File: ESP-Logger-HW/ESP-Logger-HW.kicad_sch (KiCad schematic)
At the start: 18 parts, among them J1 Conn_01x04_Male, J2 PWR, J3 USB, U1 LD33V

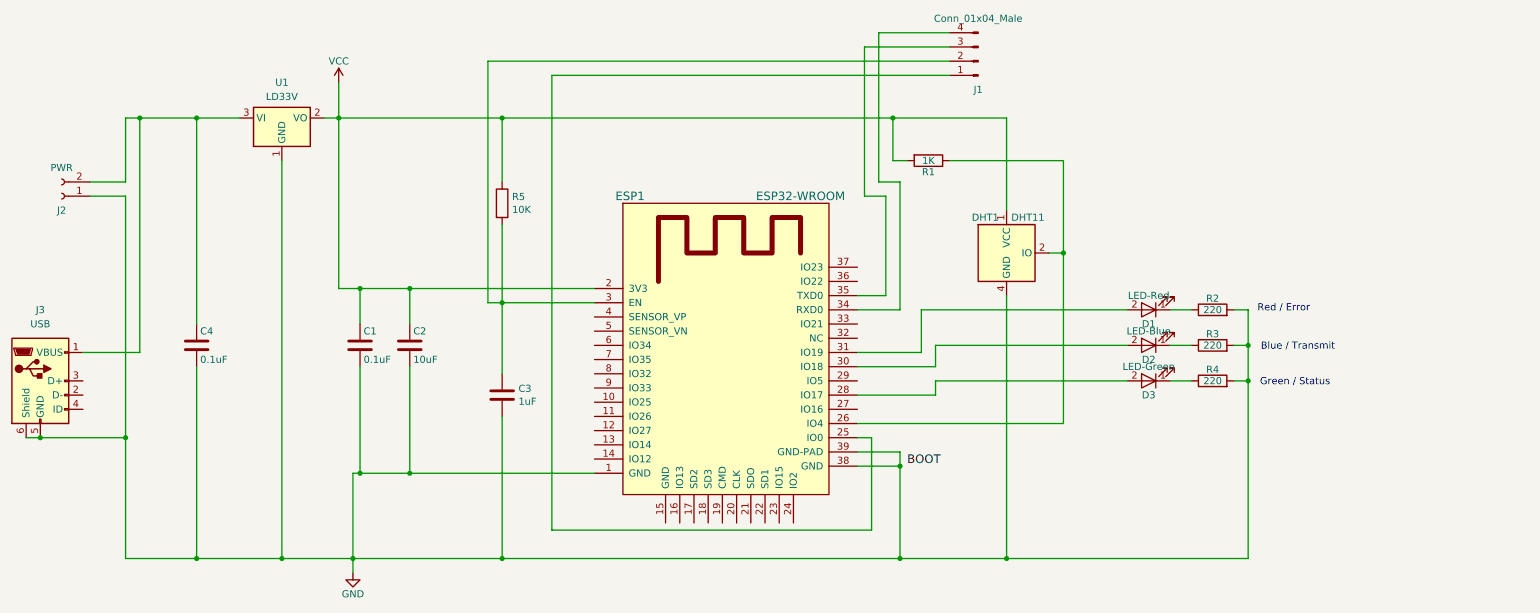
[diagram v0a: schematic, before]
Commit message: Board: Move to SHT30 temperature sensor, add option for LC-Display
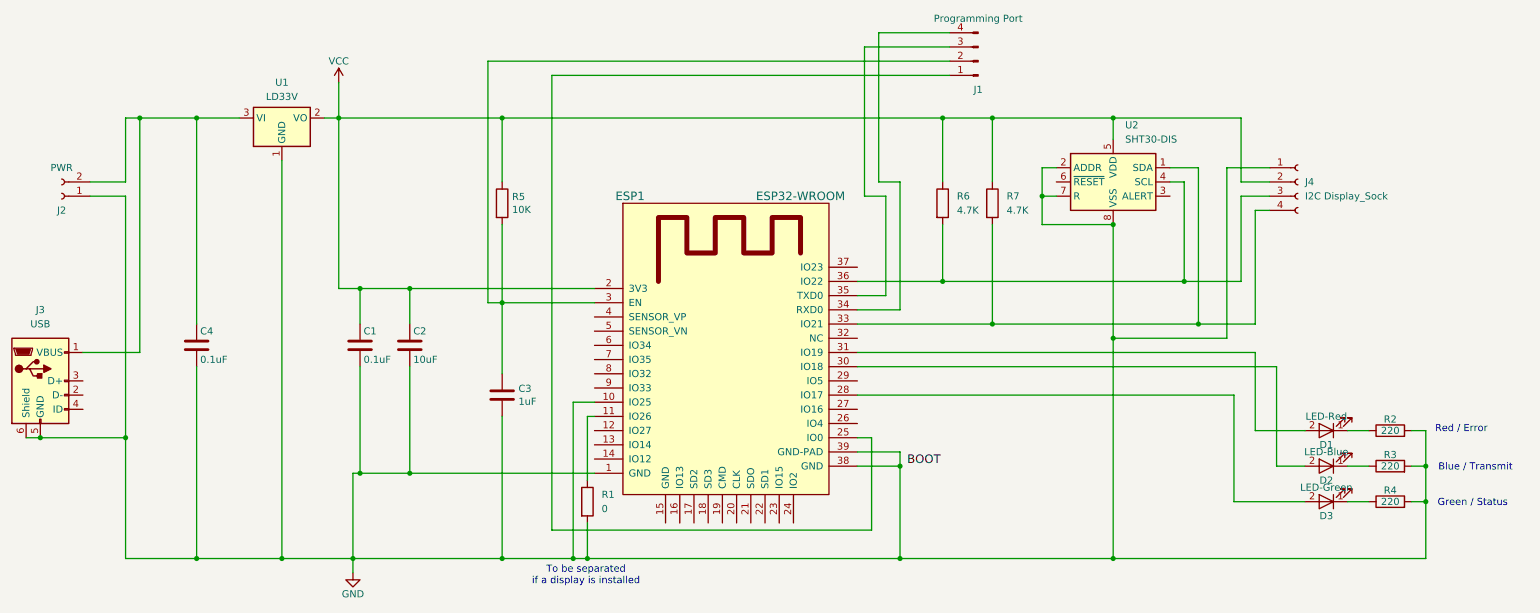
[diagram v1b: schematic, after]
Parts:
- removed DHT1: DHT11, Sensor:Aosong_DHT11_5.5x12.0_P2.54mm, symbol Sensor1:DHT11
- removed R1: 1K, Resistor_SMD:R_0603_1608Metric_Pad0.98x0.95mm_HandSolder, symbol ESP-Logger-HW-rescue:R
- added J4: I2C Display_Sock, symbol Connector:Conn_01x04_Socket
- added R1: 0, symbol Device:R
- added R6, R7: 4.7K, symbol Device:R
- added U2: SHT30-DIS, Sensor_Humidity:Sensirion_DFN-8-1EP_2.5x2.5mm_P0.5mm_EP1.1x1.7mm, symbol Sensor_Humidity:SHT30-DIS
- J1: value Conn_01x04_Male -> Programming Port
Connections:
- net GND: now also ESP1.10 (IO25), J4.1 (Pin_1), R1.2, U2.2 (ADDR), U2.7 (R), U2.8 (VSS), U2.9 (VSS)
- net VCC: now also J4.2 (Pin_2), R6.1, R7.1, U2.5 (VDD)
- net at ESP1.11 (IO26): now also R1.1
- net at ESP1.33 (IO21): now also J4.4 (Pin_4), R7.2, U2.1 (SDA)
- net at ESP1.36 (IO22): now also J4.3 (Pin_3), R6.2, U2.4 (SCL)
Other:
- note added: "To be separated if a display is installed"
- moved on the sheet: D1, D2, D3, R2, R3, R4
